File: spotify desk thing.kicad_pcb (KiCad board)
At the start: 2 copper layers, 44 parts, among them J1 AudioJack3_Ground, J2 DFR0669, J3 USB_C_Receptacle_USB2.0_16P, U1 ESP32-S3-WROOM-1-N4, U2 PCM5242RHBR, U3 EC11E18244A5, U4 TPA6132A2RTER, U9 USBLC6-2SC6

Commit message: more routing
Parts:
- added BOOT1: BOOT, EVP_AWED4A:SW_EVP-AWED4A, F.Cu at (100.0, 163.2)
- added RESET1: RESET, EVP_AWED4A:SW_EVP-AWED4A, F.Cu at (112.0, 163.2)
- J1: renamed from J2; moved to B.Cu
- moved R5 91.7 mm to (96.0, 162.8)
- moved R6 90.8 mm to (107.8, 163.0)
- moved R8 90.2 mm to (89.2, 150.2), turned to 180 degrees
- moved R7 87.1 mm to (89.2, 148.5), turned to 180 degrees
- moved C1 72.8 mm to (108.2, 164.5), turned to 180 degrees
- moved C17 65.9 mm to (149.2, 162.2)
- moved R2 61.8 mm to (119.5, 134.5)
- moved R1 54.8 mm to (119.5, 136.2)
- moved C12 53.5 mm to (115.8, 151.0), turned to -90 degrees
- turned J1 to 180 degrees
- renumbered C19 to C1, C12 to C10, C7 to C11, C6 to C12, C8 to C15, C11 to C16, C5 to C17, C1 to C18, C2 to C19, C10 to C2, C4 to C3, C18 to C4, C17 to C5, C16 to C6, C15 to C7, C9 to C8, C3 to C9, J1 to J2, R4 to R1, R11 to R10, R8 to R11, R10 to R13, R9 to R14, R5 to R2, R14 to R3, R13 to R4, R3 to R5, R1 to R6, R6 to R8, R2 to R9, U4 to U2, U2 to U3, U3 to U4, U9 to U5
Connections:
- U1 pad 41_19: (no net) -> DGND
- U1 pad 41_21: (no net) -> DGND
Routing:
- net SCL: track 0.00 -> 131.6 mm, vias 0 -> 4
- net 5v: track 26.1 -> 145.0 mm, vias 0 -> 2
- net SDA: track 0.00 -> 111.0 mm, vias 0 -> 4
- net SD_CS: track 0.00 -> 86.2 mm, vias 0 -> 1
- net TOUCH_INT: track 0.00 -> 82.9 mm, vias 0 -> 2
- net SCREEN_BL: track 0.00 -> 79.5 mm, vias 0 -> 1
- net SCREEN_MOSI: track 0.00 -> 60.5 mm
- net SCREEN_DC: track 0.00 -> 58.4 mm
- net 3.3v: track 76.9 -> 135.2 mm, vias 10 -> 13
- net SCREEN_MISO: track 0.00 -> 57.1 mm
- net SCREEN_RES: track 0.00 -> 56.7 mm, vias 0 -> 1
- net SCREEN_CS: track 0.00 -> 56.6 mm
- net SCREEN_SCLK: track 0.00 -> 55.5 mm
- net USB_D-: track 0.00 -> 51.4 mm, vias 0 -> 2
- net USB_D+: track 0.00 -> 50.7 mm, vias 0 -> 2
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- added copper zone on F.Cu, net DGND
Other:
- board outline added: 120.5 x 50 mm
- rule pad_to_mask_clearance: 0 -> 0.1

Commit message: updated stuff to jlc thing
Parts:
- removed the J2 at (128.0, 168.0)
- added J1: AudioJack3_Ground, SJ_3523_SMT_TR:CUI_SJ-3523-SMT-TR, F.Cu at (128.0, 168.6)
- BOOT1, RESET1: footprint EVP_AWED4A:SW_EVP-AWED4A -> Button_Switch_SMD:SW_SPST_CK_KMS2xxG
- C12: renamed from C14; value 1.1uF -> 1uF; footprint Capacitor_SMD:C_0402_1005Metric -> Capacitor_SMD:C_0603_1608Metric
- moved J3 8.50 mm to (50.0, 135.5)
- moved RESET1 3.58 mm to (113.5, 166.5)
- moved BOOT1 3.31 mm to (100.2, 166.6)
- moved C12 0.23 mm to (124.8, 153.5)
- renumbered C8 to C10, C10 to C11, C9 to C13, C12 to C14, C13 to C15, C15 to C16, C3 to C2, C16 to C3, C2 to C6, C6 to C7, C7 to C8, C11 to C9, J3 to J2, J1 to J3, R2 to R1, R1 to R2, R4 to R3, R3 to R4, R6 to R5, R7 to R6, R5 to R7
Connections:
- U1 pad 41_19: DGND -> (no net)
- U1 pad 41_21: DGND -> (no net)
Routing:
- net SD_CS: track 86.2 -> 76.9 mm
- net SCREEN_DC: track 58.4 -> 49.7 mm
- net SCREEN_RES: track 56.7 -> 48.1 mm
- net SCL: track 131.6 -> 123.2 mm
- net SCREEN_CS: track 56.6 -> 48.1 mm
- net SCREEN_MISO: track 57.1 -> 48.7 mm
- net SCREEN_SCLK: track 55.5 -> 47.1 mm
- net SCREEN_BL: track 79.5 -> 71.7 mm
- net SDA: track 111.0 -> 103.4 mm
- net Net-(U1-EN): track 19.5 -> 26.7 mm
- net SCREEN_MOSI: track 60.5 -> 53.6 mm
- net DGND: track 47.2 -> 40.4 mm, vias 25 -> 21
- net 5v: track 145.0 -> 138.9 mm, vias 2 -> 4
- net Net-(U1-IO0): track 33.5 -> 39.4 mm
- net TOUCH_INT: track 82.9 -> 80.5 mm
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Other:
- board size 120.5 x 50 mm -> 113 x 50 mm
- rule pad_to_mask_clearance: 0.1 -> 0
- board text added: "Spotify Desk Thing v1 blazecoding.xyz Hack Club Blueprint"

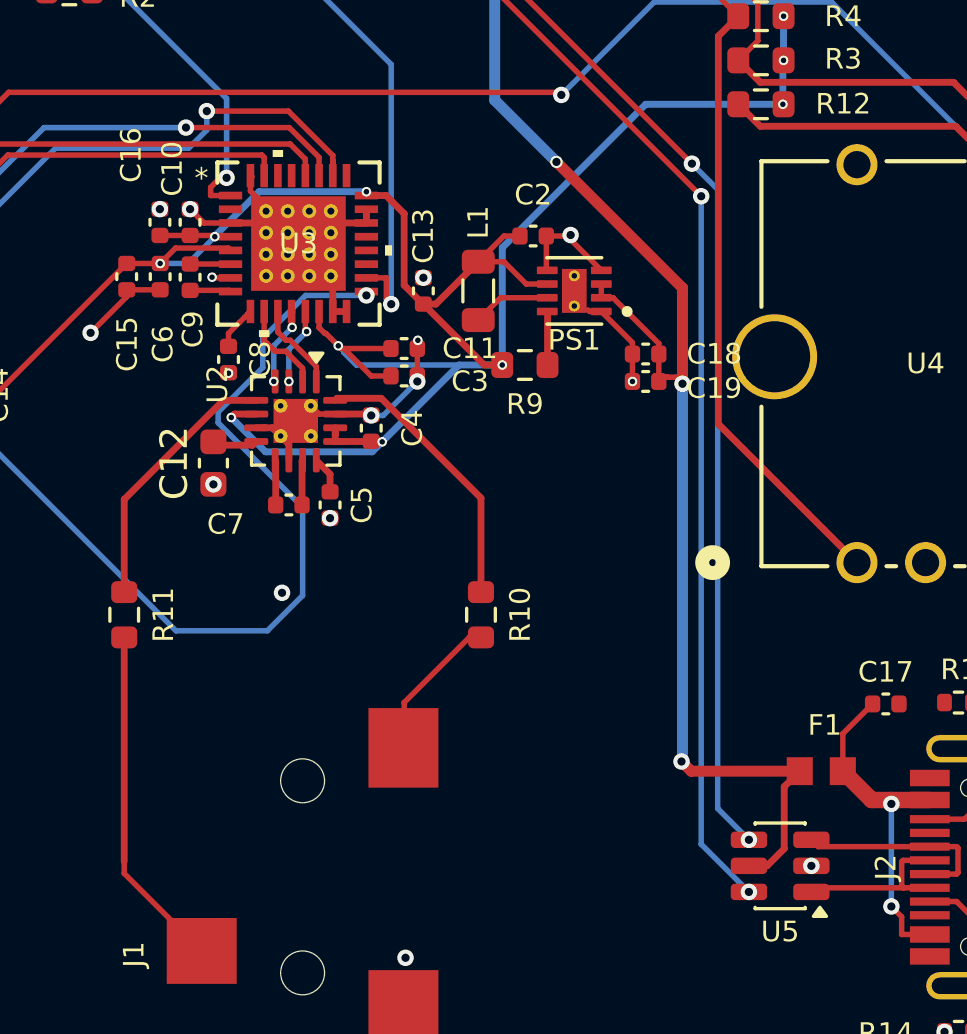
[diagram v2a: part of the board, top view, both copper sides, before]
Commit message: fixed some errors
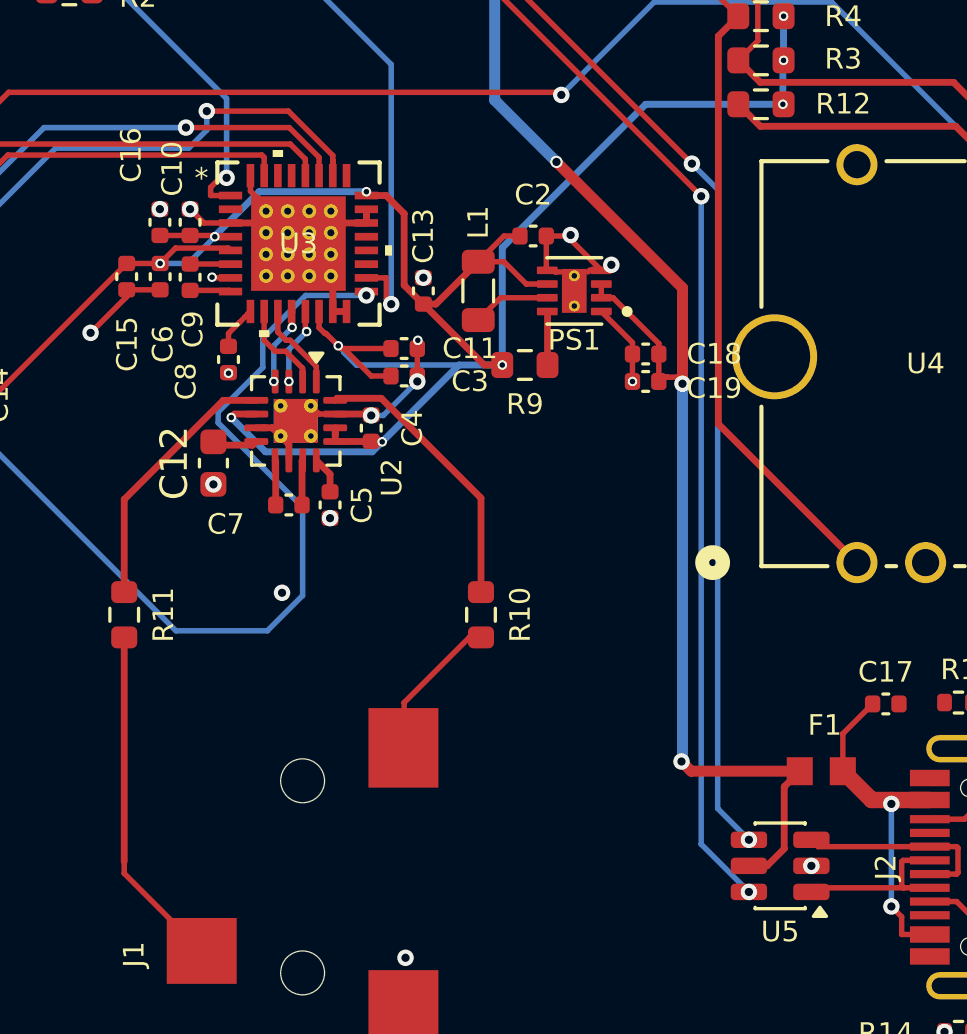
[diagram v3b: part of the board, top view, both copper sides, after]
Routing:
- net 5v: track 138.9 -> 138.1 mm
- net DGND: track 40.4 -> 40.9 mm, vias 21 -> 22
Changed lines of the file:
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@@
 		(tags "capacitor")
 		(property "Reference" "C8"
-			(at 0 -1.16 90)
+			(at 0.8 1.55 90)
 			(layer "F.SilkS")
 			(effects
@@
 		(tags "WQFN NoLead")
 		(property "Reference" "U2"
-			(at -1.3375 2.85 90)
+			(at 2.0625 -3.5 90)
 			(layer "F.SilkS")
 			(effects
@@
 	)
 	(segment
+		(start 138.46 146.45)
+		(end 138.401 146.509)
+		(width 0.2)
+		(layer "F.Cu")
+		(net 1)
+	)
+	(segment
 		(start 128.3 151.388)
 		(end 128.6 151.688)
@@
 	)
 	(segment
-		(start 138.885 147.95)
-		(end 138.46 147.95)
-		(width 0.2)
-		(layer "F.Cu")
-		(net 1)
-	)
-	(segment
 		(start 126.338 143.804)
 		(end 126.258 143.884)
@@
 	)
 	(segment
+		(start 137.15 146.45)
+		(end 137.209 146.509)
+		(width 0.2)
+		(layer "F.Cu")
+		(net 1)
+	)
+	(segment
 		(start 137.635 145.2)
 		(end 138.885 146.45)
@@
 	)
 	(segment
-		(start 138.885 147.95)
-		(end 140.02 149.085)
+		(start 138.885 146.45)
+		(end 138.46 146.45)
 		(width 0.2)
 		(layer "F.Cu")
@@
 	)
 	(segment
-		(start 121.59 147.413)
-		(end 121.59 147.16)
+		(start 138.885 147.95)
+		(end 140.02 149.085)
 		(width 0.2)
 		(layer "F.Cu")
@@
 	)
 	(segment
-		(start 138.46 147.95)
-		(end 138.401 147.891)
+		(start 121.59 147.413)
+		(end 121.59 147.16)
 		(width 0.2)
 		(layer "F.Cu")
@@
 	)
 	(segment
+		(start 136.915 146.45)
+		(end 137.15 146.45)
+		(width 0.2)
+		(layer "F.Cu")
+		(net 1)
+	)
+	(segment
 		(start 130.325 144.475)
 		(end 130.325 144.725)
@@
 	)
 	(segment
-		(start 126.099 143)
-		(end 126.133 143.034)
-		(width 0.25)
+		(start 137.209 146.509)
+		(end 137.399 146.509)
+		(width 0.2)
 		(layer "F.Cu")
 		(net 1)
@@
 	)
 	(via
+		(at 139.25 146.25)
+		(size 0.6)
+		(drill 0.3)
+		(layers "F.Cu" "B.Cu")
+		(free yes)
+		(net 1)
+	)
+	(via
 		(at 125.3 150.2)
 		(size 0.35)
@@
 	)
 	(segment
-		(start 144.2625 168.15)
-		(end 144.262 168.15)
-		(width 0.25)
-		(layer "F.Cu")
-		(net 2)
-	)
-	(segment
 		(start 138.885 147.45)
 		(end 139.311 147.45)
@@
 	)
 	(segment
-		(start 146.115 164.7)
-		(end 145.338 164.7)
-		(width 0.2)
-		(layer "F.Cu")
-		(net 2)
-	)
-	(segment
 		(start 145.549 167.526)
 		(end 144.925 168.15)
@@
 	)
 	(segment
-		(start 125.3746 145.225)
-		(end 125.375 145.225)
-		(width 0.25)
-		(layer "F.Cu")
-		(net 3)
-	)
-	(segment
 		(start 125.3746 145.725)
 		(end 125.3748 145.7248)
@@
 	)
 	(segment
-		(start 125.3748 145.7248)
-		(end 125.375 145.725)
-		(width 0.2)
-		(layer "F.Cu")
-		(net 3)
-	)
-	(segment
 		(start 113.58 150.52)
 		(end 113.35 150.29)
@@
 	)
 	(segment
-		(start 125.375 143.725)
-		(end 125.3746 143.725)
-		(width 0.2)
-		(layer "F.Cu")
-		(net 26)
-	)
-	(segment
 		(start 125.3746 143.725)
 		(end 124.648 143.725)
@@
 	(segment
 		(start 128.1 142.7)
-		(end 128.1 143)
-		(width 0.2)
-		(layer "F.Cu")
-		(net 56)
-	)
-	(segment
-		(start 128.1 142.7)
 		(end 128.1 142.4)
 		(width 0.2)
@@
 	)
 	(segment
-		(start 125.372 146.222)
-		(end 125.3735 146.2235)
-		(width 0.2)
-		(layer "F.Cu")
-		(net 61)
-	)
-	(segment
 		(start 125.37 146.22)
 		(end 125.372 146.222)
@@
 		(width 0.2)
 		(layer "F.Cu")
-		(net 65)
-	)
-	(segment
-		(start 129.206 151.17)
-		(end 129.188 151.188)
-		(width 0.2)
-		(layer "F.Cu")

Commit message: cleanup
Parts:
- moved R10 39.1 mm to (141.0, 168.9)
- moved R9 39.1 mm to (141.0, 167.2)
- moved R12 23.9 mm to (96.0, 171.4), turned to -90 degrees
- moved R13 22.8 mm to (97.8, 171.4), turned to -90 degrees
- moved BOOT1 21.6 mm to (102.1, 145.1)
- moved RESET1 21.6 mm to (115.4, 145.0)
- moved R4 21.3 mm to (107.2, 144.6), turned to 180 degrees
- moved C4 18.7 mm to (111.2, 146.0)
- moved R5 18.7 mm to (111.0, 144.6)
- moved C19 16.6 mm to (119.7, 167.2)
- moved U4 16.6 mm to (108.5, 162.5)
- moved R11 11.8 mm to (121.2, 170.8)
- moved C17 2.03 mm to (125.4, 155.4)
- moved C9 1.58 mm to (124.0, 148.8)
- renumbered C16 to C1, C11 to C10, C18 to C11, C3 to C12, C19 to C13, C4 to C14, C7 to C15, C5 to C16, C12 to C17, C17 to C18, C14 to C19, C10 to C2, C2 to C3, C1 to C4, C15 to C5, C9 to C7, C13 to C8, C8 to C9, J2 to J1, J1 to J2, R4 to R1, R2 to R10, R6 to R12, R8 to R13, R3 to R2, R12 to R3, R7 to R4, R9 to R6, R10 to R7, R13 to R8, R1 to R9, U3 to U1, U4 to U3, U1 to U4
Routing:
- net USB_D-: track 51.4 -> 2.61 mm, vias 2 -> 0
- net USB_D+: track 50.7 -> 2.44 mm, vias 2 -> 0
- net Net-(U1-IO20): track 5.55 -> 33.3 mm
- net Net-(U1-IO19): track 5.35 -> 32.8 mm
- net Net-(U1-IO0): track 39.4 -> 14.4 mm
- net SCREEN_SCLK: track 47.1 -> 65.4 mm
- net SCL: track 123.2 -> 105.7 mm, vias 4 -> 3
- net DGND: track 40.9 -> 55.9 mm, vias 22 -> 13
- net SD_CS: track 76.9 -> 62.3 mm
- net ENC_B: track 76.4 -> 64.2 mm
- net I2S_DOUT: track 16.4 -> 28.4 mm, vias 0 -> 2
- net Net-(U2-OUTR): track 9.68 -> 21.5 mm, vias 0 -> 2
- net SCREEN_MISO: track 48.7 -> 60.5 mm
- net SCREEN_MOSI: track 53.6 -> 64.6 mm, vias 0 -> 1
- net SCREEN_RES: track 48.1 -> 59.0 mm
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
